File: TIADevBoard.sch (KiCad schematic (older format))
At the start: 30 parts, among them J1 Screw_Terminal_01x02, J2 Conn_Coaxial, J3 Conn_Coaxial, U1 MC33063AD, U2 OPA2387, U3 ADP3330-3, U4 ADP7183

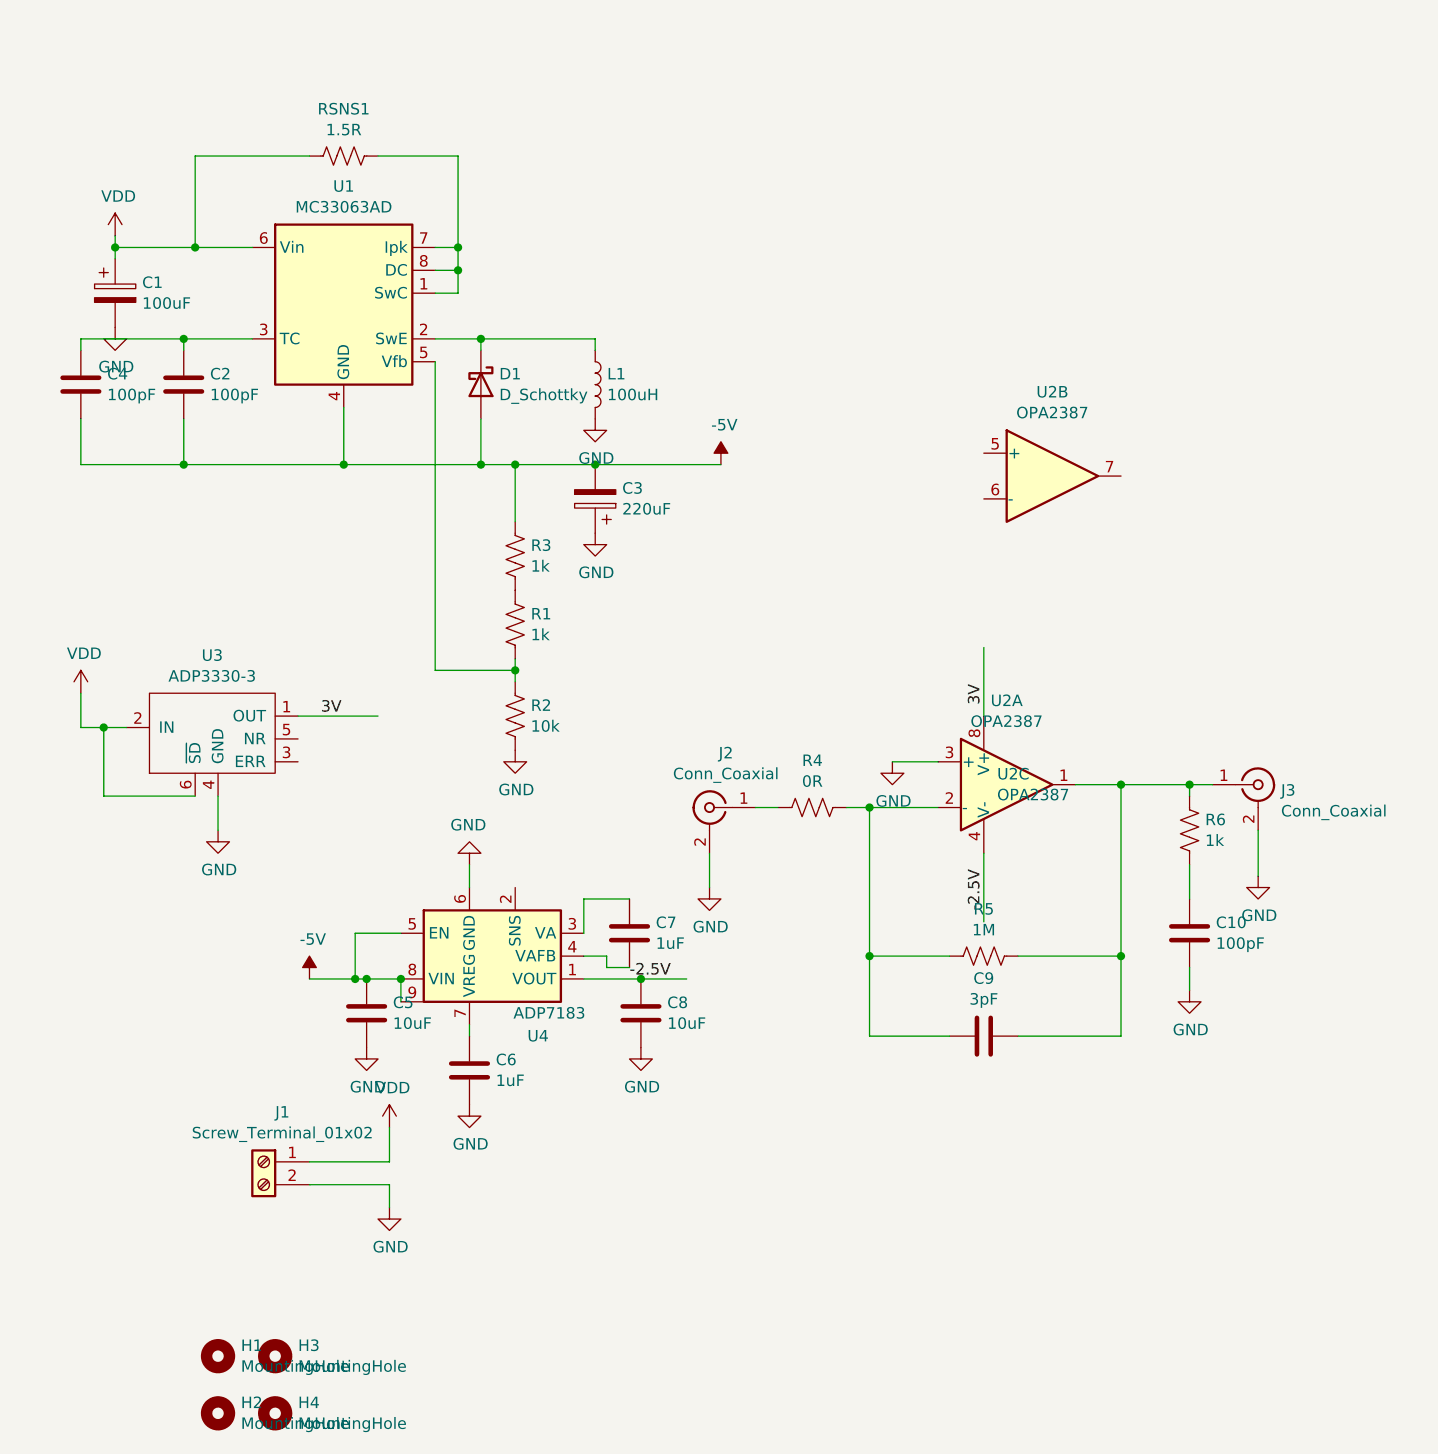
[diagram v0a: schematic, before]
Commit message: Version 3 complete with +3V/-2.5V low noise LDO regulated supplies, a -5V inverting DC switching converter, and a new low-noise TIA
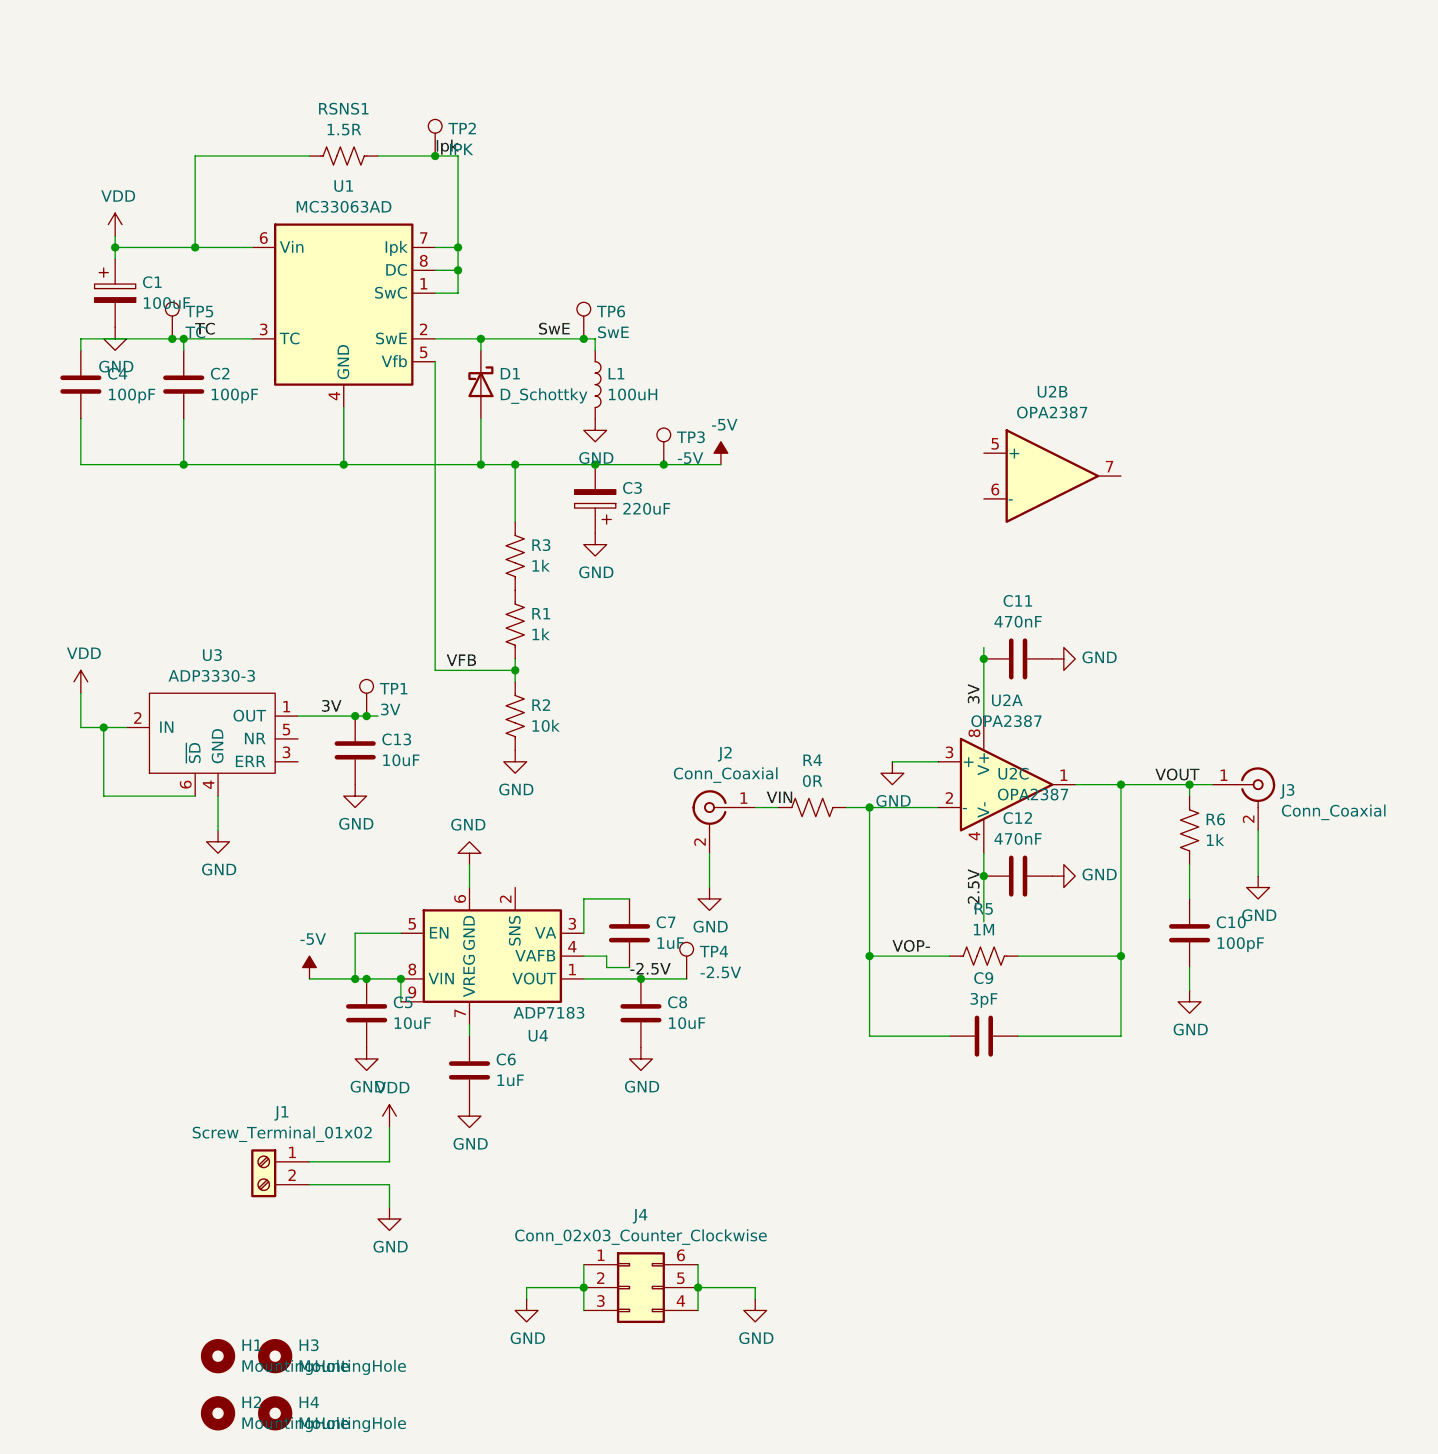
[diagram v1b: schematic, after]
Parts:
- added C11, C12: 470nF, Capacitor_SMD:C_0805_2012Metric_Pad1.15x1.40mm_HandSolder, symbol Device:C
- added C13: 10uF, Capacitor_SMD:C_0805_2012Metric_Pad1.15x1.40mm_HandSolder, symbol Device:C
- added J4: Conn_02x03_Counter_Clockwise, Connector_PinHeader_2.54mm:PinHeader_2x03_P2.54mm_Vertical, symbol Connector_Generic:Conn_02x03_Counter_Clockwise
- added TP1: 3V, my_library_foot:TestPoint_Keystone_5000-5004_Miniature, symbol Connector:TestPoint
- added TP2: IPK, my_library_foot:TestPoint_Keystone_5000-5004_Miniature, symbol Connector:TestPoint
- added TP3: -5V, my_library_foot:TestPoint_Keystone_5000-5004_Miniature, symbol Connector:TestPoint
- added TP4: -2.5V, my_library_foot:TestPoint_Keystone_5000-5004_Miniature, symbol Connector:TestPoint
- added TP5: TC, my_library_foot:TestPoint_Keystone_5000-5004_Miniature, symbol Connector:TestPoint
- added TP6: SwE, my_library_foot:TestPoint_Keystone_5000-5004_Miniature, symbol Connector:TestPoint
- J1: footprint TerminalBlock_4Ucon:TerminalBlock_4Ucon_1x02_P3.50mm_Vertical -> TerminalBlock:TerminalBlock_Altech_AK300-2_P5.00mm
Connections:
- net labels added: Ipk, SwE, TC, VFB, VIN, VOP-, VOUT
- wire segments 84 -> 100
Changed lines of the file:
@@
 F 0 "J1" H 1718 5767 50  0000 C CNN
 F 1 "Screw_Terminal_01x02" H 1718 5676 50  0000 C CNN
-F 2 "TerminalBlock_4Ucon:TerminalBlock_4Ucon_1x02_P3.50mm_Vertical" H 1800 5550 50  0001 C CNN
+F 2 "TerminalBlock:TerminalBlock_Altech_AK300-2_P5.00mm" H 1800 5550 50  0001 C CNN
 F 3 "~" H 1800 5550 50  0001 C CNN
 	1    1800 5550
@@
 	2650 1550 2650 1150
 Wire Wire Line
-	2650 1150 2300 1150
+	2650 1150 2550 1150
 Connection ~ 2650 1550
 Wire Wire Line
@@
 	3250 2000 3250 1950
 Wire Wire Line
-	3250 1950 2750 1950
+	3250 1950 3200 1950
 Connection ~ 2750 1950
 $Comp
@@
 $EndComp
 Wire Wire Line
-	3250 2500 3800 2500
+	3250 2500 3550 2500
 $Comp
 L Device:R_US R3
@@
 	1000 2000 1000 1950
 Wire Wire Line
-	1000 1950 1450 1950
+	1000 1950 1400 1950
 Connection ~ 1450 1950
 Wire Wire Line
@@
 $EndComp
 Wire Wire Line
-	4950 3600 4950 3300
+	4950 3600 4950 3350
 Text Label 4950 3550 1    50   ~ 0
 3V
 Wire Wire Line
-	4950 4200 4950 4500
+	4950 4200 4950 4300
 Text Label 4950 4450 1    50   ~ 0
 -2.5V
@@
 	1100 3650 1200 3650
 Wire Wire Line
-	1950 3600 2300 3600
+	1950 3600 2200 3600
 Text Label 2050 3600 0    50   ~ 0
 3V
@@
 	2400 4850 2400 4750
 Connection ~ 2400 4750
+Text Label 4000 4000 0    50   ~ 0
+VIN
+Text Label 5700 3900 0    50   ~ 0
+VOUT
+Text Label 4550 4650 0    50   ~ 0
+VOP-
+Text Label 2550 1150 0    50   ~ 0
+Ipk
+Text Label 1500 1950 0    50   ~ 0
+TC
+Text Label 2600 3400 0    50   ~ 0
+VFB
+Text Label 3000 1950 0    50   ~ 0
+SwE
+$Comp
+L Device:C C11
+U 1 1 6002D9D3
+P 5100 3350
+F 0 "C11" V 4848 3350 50  0000 C CNN
+F 1 "470nF" V 4939 3350 50  0000 C CNN
+F 2 "Capacitor_SMD:C_0805_2012Metric_Pad1.15x1.40mm_HandSolder" H 5138 3200 50  0001 C CNN
+F 3 "~" H 5100 3350 50  0001 C CNN
+	1    5100 3350
+	0    1    1    0
+$EndComp
+Connection ~ 4950 3350
+Wire Wire Line
+	4950 3350 4950 3300
+$Comp
+L power:GND #PWR012
+U 1 1 6002F15E
+P 5250 3350
+F 0 "#PWR012" H 5250 3100 50  0001 C CNN
+F 1 "GND" V 5255 3222 50  0000 R CNN
+F 2 "" H 5250 3350 50  0001 C CNN
+F 3 "" H 5250 3350 50  0001 C CNN
+	1    5250 3350
+	0    -1   -1   0
+$EndComp
+$Comp
+L Device:C C12
+U 1 1 6002FB84
+P 5100 4300
+F 0 "C12" V 5352 4300 50  0000 C CNN
+F 1 "470nF" V 5261 4300 50  0000 C CNN
+F 2 "Capacitor_SMD:C_0805_2012Metric_Pad1.15x1.40mm_HandSolder" H 5138 4150 50  0001 C CNN
+F 3 "~" H 5100 4300 50  0001 C CNN
+	1    5100 4300
+	0    -1   -1   0
+$EndComp
+Connection ~ 4950 4300
+Wire Wire Line
+	4950 4300 4950 4500
+$Comp
+L power:GND #PWR013
+U 1 1 60030758
+P 5250 4300
+F 0 "#PWR013" H 5250 4050 50  0001 C CNN
+F 1 "GND" V 5255 4172 50  0000 R CNN
+F 2 "" H 5250 4300 50  0001 C CNN
+F 3 "" H 5250 4300 50  0001 C CNN
+	1    5250 4300
+	0    -1   -1   0
+$EndComp
+$Comp
+L Device:C C13
+U 1 1 60071AFA
+P 2200 3750
+F 0 "C13" H 2315 3796 50  0000 L CNN
+F 1 "10uF" H 2315 3705 50  0000 L CNN
+F 2 "Capacitor_SMD:C_0805_2012Metric_Pad1.15x1.40mm_HandSolder" H 2238 3600 50  0001 C CNN
+F 3 "~" H 2200 3750 50  0001 C CNN
+	1    2200 3750
+	1    0    0    -1
+$EndComp
+Connection ~ 2200 3600
+Wire Wire Line
+	2200 3600 2250 3600
+$Comp
+L power:GND #PWR0109
+U 1 1 600724B2
+P 2200 3900
+F 0 "#PWR0109" H 2200 3650 50  0001 C CNN
+F 1 "GND" H 2205 3727 50  0000 C CNN
+F 2 "" H 2200 3900 50  0001 C CNN
+F 3 "" H 2200 3900 50  0001 C CNN
+	1    2200 3900
+	1    0    0    -1
+$EndComp
+$Comp
+L Connector:TestPoint TP1
+U 1 1 600D003D
+P 2250 3600
+F 0 "TP1" H 2308 3718 50  0000 L CNN
+F 1 "3V" H 2308 3627 50  0000 L CNN
+F 2 "my_library_foot:TestPoint_Keystone_5000-5004_Miniature" H 2450 3600 50  0001 C CNN
+F 3 "~" H 2450 3600 50  0001 C CNN
+	1    2250 3600
+	1    0    0    -1
+$EndComp
+Connection ~ 2250 3600
+Wire Wire Line
+	2250 3600 2300 3600
+$Comp
+L Connector:TestPoint TP3
+U 1 1 600D12C3
+P 3550 2500
+F 0 "TP3" H 3608 2618 50  0000 L CNN
+F 1 "-5V" H 3608 2527 50  0000 L CNN
+F 2 "my_library_foot:TestPoint_Keystone_5000-5004_Miniature" H 3750 2500 50  0001 C CNN
+F 3 "~" H 3750 2500 50  0001 C CNN
+	1    3550 2500
+	1    0    0    -1
+$EndComp
+Connection ~ 3550 2500
+Wire Wire Line
+	3550 2500 3800 2500
+$Comp
+L Connector:TestPoint TP4
+U 1 1 600D1DA7
+P 3650 4750
+F 0 "TP4" H 3708 4868 50  0000 L CNN
+F 1 "-2.5V" H 3708 4777 50  0000 L CNN
+F 2 "my_library_foot:TestPoint_Keystone_5000-5004_Miniature" H 3850 4750 50  0001 C CNN
+F 3 "~" H 3850 4750 50  0001 C CNN
+	1    3650 4750
+	1    0    0    -1
+$EndComp
+$Comp
+L Connector:TestPoint TP2
+U 1 1 600D27CC
+P 2550 1150
+F 0 "TP2" H 2608 1268 50  0000 L CNN
+F 1 "IPK" H 2608 1177 50  0000 L CNN
+F 2 "my_library_foot:TestPoint_Keystone_5000-5004_Miniature" H 2750 1150 50  0001 C CNN
+F 3 "~" H 2750 1150 50  0001 C CNN
+	1    2550 1150
+	1    0    0    -1
+$EndComp
+Connection ~ 2550 1150
+Wire Wire Line
+	2550 1150 2300 1150
+$Comp
+L Connector:TestPoint TP6
+U 1 1 600D9614
+P 3200 1950
+F 0 "TP6" H 3258 2068 50  0000 L CNN
+F 1 "SwE" H 3258 1977 50  0000 L CNN
+F 2 "my_library_foot:TestPoint_Keystone_5000-5004_Miniature" H 3400 1950 50  0001 C CNN
+F 3 "~" H 3400 1950 50  0001 C CNN
+	1    3200 1950
+	1    0    0    -1
+$EndComp
+Connection ~ 3200 1950
+Wire Wire Line
+	3200 1950 2750 1950
+$Comp
+L Connector:TestPoint TP5
+U 1 1 600DA27F
+P 1400 1950
+F 0 "TP5" H 1458 2068 50  0000 L CNN
+F 1 "TC" H 1458 1977 50  0000 L CNN
+F 2 "my_library_foot:TestPoint_Keystone_5000-5004_Miniature" H 1600 1950 50  0001 C CNN
+F 3 "~" H 1600 1950 50  0001 C CNN
+	1    1400 1950
+	1    0    0    -1
+$EndComp
+Connection ~ 1400 1950
+Wire Wire Line
+	1400 1950 1450 1950
+$Comp
+L Connector_Generic:Conn_02x03_Counter_Clockwise J4
+U 1 1 600F320C
+P 3400 6100
+F 0 "J4" H 3450 6417 50  0000 C CNN
+F 1 "Conn_02x03_Counter_Clockwise" H 3450 6326 50  0000 C CNN
+F 2 "Connector_PinHeader_2.54mm:PinHeader_2x03_P2.54mm_Vertical" H 3400 6100 50  0001 C CNN
+F 3 "~" H 3400 6100 50  0001 C CNN
+	1    3400 6100
+	1    0    0    -1
+$EndComp
+$Comp
+L power:GND #PWR0110
+U 1 1 600F48E6
+P 2950 6150
+F 0 "#PWR0110" H 2950 5900 50  0001 C CNN
+F 1 "GND" H 2955 5977 50  0000 C CNN
+F 2 "" H 2950 6150 50  0001 C CNN
+F 3 "" H 2950 6150 50  0001 C CNN
+	1    2950 6150
+	1    0    0    -1
+$EndComp
+Wire Wire Line
+	3200 6000 3200 6100
+Connection ~ 3200 6100
+Wire Wire Line
+	3200 6100 3200 6200
+Wire Wire Line
+	3200 6100 2950 6100
+Wire Wire Line
+	2950 6100 2950 6150
+$Comp
+L power:GND #PWR0111
+U 1 1 600FA4B1
+P 3950 6150
+F 0 "#PWR0111" H 3950 5900 50  0001 C CNN
+F 1 "GND" H 3955 5977 50  0000 C CNN
+F 2 "" H 3950 6150 50  0001 C CNN
+F 3 "" H 3950 6150 50  0001 C CNN
+	1    3950 6150
+	1    0    0    -1
+$EndComp
+Wire Wire Line
+	3700 6000 3700 6100
+Connection ~ 3700 6100
+Wire Wire Line
+	3700 6100 3700 6200
+Wire Wire Line
+	3700 6100 3950 6100
+Wire Wire Line
+	3950 6100 3950 6150
 $EndSCHEMATC

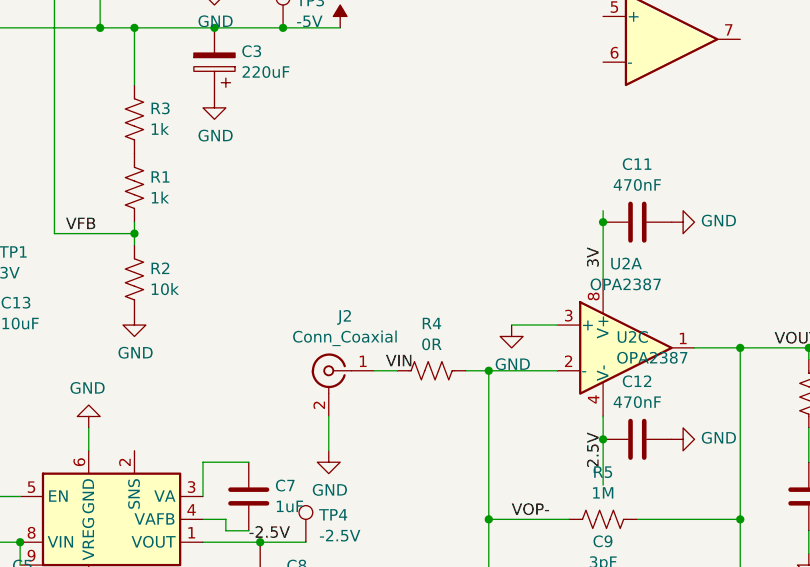
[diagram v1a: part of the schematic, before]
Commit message: added second SMA connector for Vin+ terminal
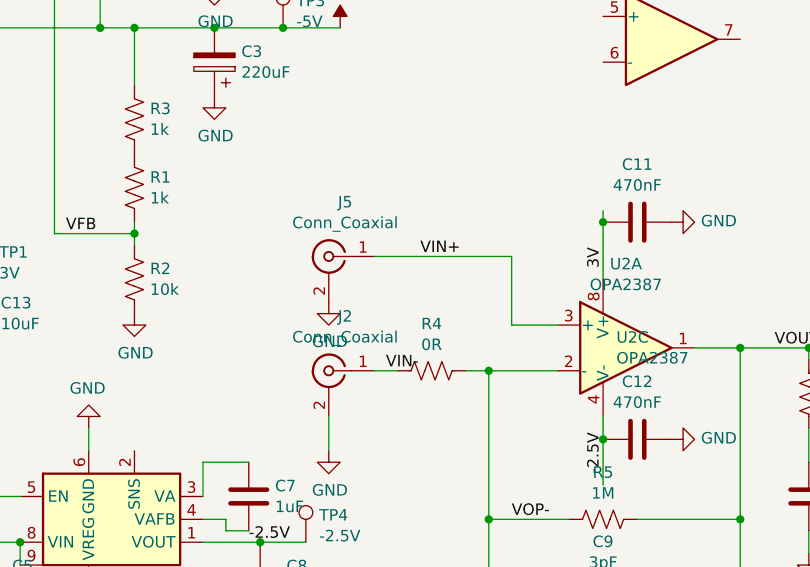
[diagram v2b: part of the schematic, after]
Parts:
- added J5: Conn_Coaxial, my_library_foot:CON-SMA-EDGE-S, symbol Connector:Conn_Coaxial
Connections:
- net labels added: VIN+, VIN-
- net labels removed: VIN
- wire segments 100 -> 102
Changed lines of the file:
@@
 Wire Wire Line
 	5350 3900 5550 3900
-$Comp
-L power:GND #PWR09
-U 1 1 600680C3
-P 4550 3800
-F 0 "#PWR09" H 4550 3550 50  0001 C CNN
-F 1 "GND" H 4555 3627 50  0000 C CNN
-F 2 "" H 4550 3800 50  0001 C CNN
-F 3 "" H 4550 3800 50  0001 C CNN
-	1    4550 3800
-	1    0    0    -1
-$EndComp
 Wire Wire Line
 	4550 3800 4750 3800
@@
 Connection ~ 2400 4750
 Text Label 4000 4000 0    50   ~ 0
-VIN
+VIN-
 Text Label 5700 3900 0    50   ~ 0
 VOUT
@@
 Wire Wire Line
 	3950 6100 3950 6150
+$Comp
+L Connector:Conn_Coaxial J5
+U 1 1 60138FFA
+P 3750 3500
+F 0 "J5" H 3678 3738 50  0000 C CNN
+F 1 "Conn_Coaxial" H 3678 3647 50  0000 C CNN
+F 2 "my_library_foot:CON-SMA-EDGE-S" H 3750 3500 50  0001 C CNN
+F 3 " ~" H 3750 3500 50  0001 C CNN
+	1    3750 3500
+	-1   0    0    -1
+$EndComp
+$Comp
+L power:GND #PWR09
+U 1 1 60139F50
+P 3750 3700
+F 0 "#PWR09" H 3750 3450 50  0001 C CNN
+F 1 "GND" H 3755 3527 50  0000 C CNN
+F 2 "" H 3750 3700 50  0001 C CNN
+F 3 "" H 3750 3700 50  0001 C CNN
+	1    3750 3700
+	1    0    0    -1
+$EndComp
+Wire Wire Line
+	3950 3500 4550 3500
+Wire Wire Line
+	4550 3500 4550 3800
+Text Label 4150 3500 0    50   ~ 0
+VIN+
 $EndSCHEMATC
